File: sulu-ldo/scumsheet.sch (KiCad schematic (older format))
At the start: 19 parts, among them J10 through_hole, J11 through_hole, J12 through_hole, J13 through_hole, J14 through_hole, J15 through_hole, J16 through_hole, J17 through_hole, J18 through_hole, J19 through_hole, J20 through_hole, J21 through_hole, J5 through_hole, J6 through_hole, J7 through_hole, J8 through_hole, J9 through_hole, U1 scum3

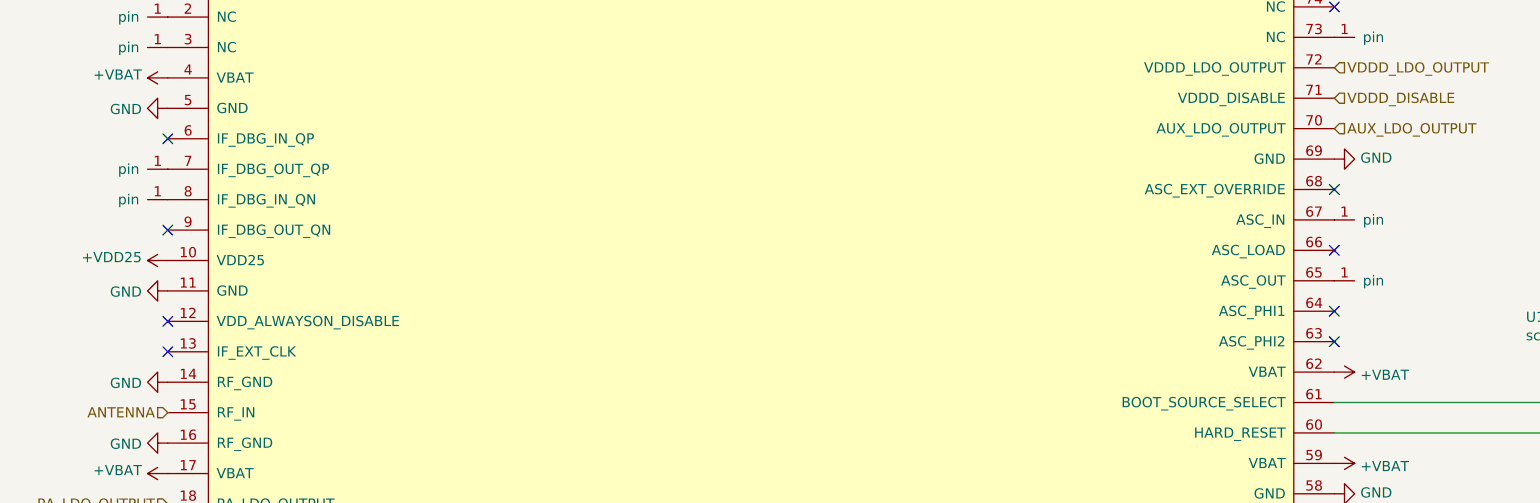
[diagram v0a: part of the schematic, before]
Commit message: added ldos
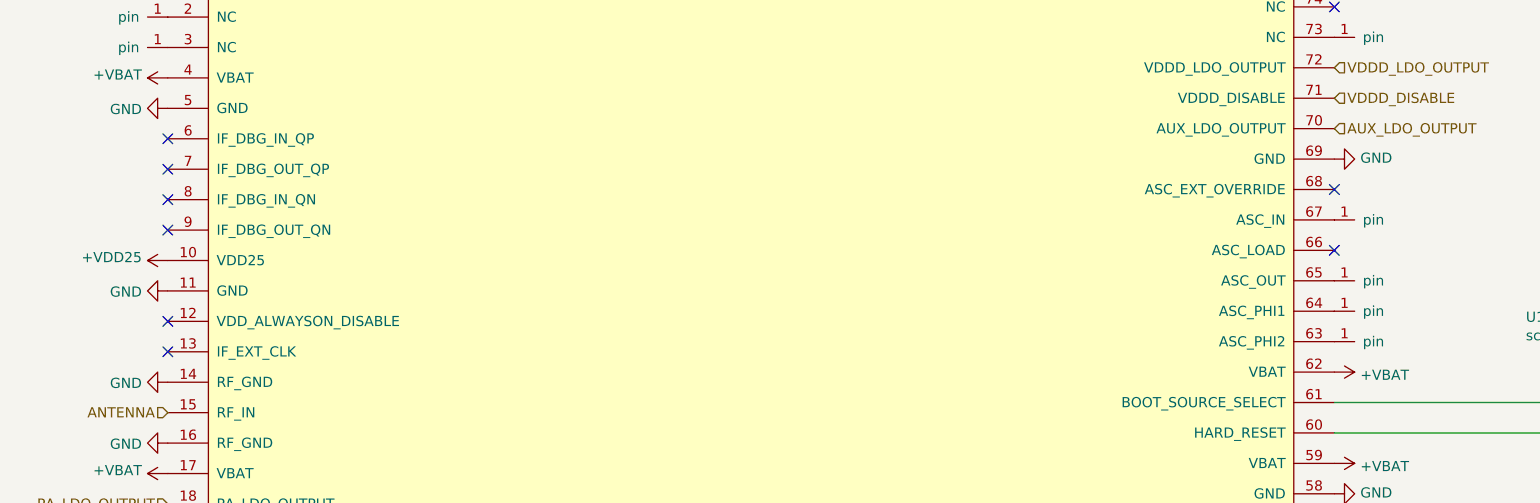
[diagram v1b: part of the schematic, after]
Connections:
- net at U1.63 (ASC_PHI2): now also J9.1 (pin)
- net at U1.64 (ASC_PHI1): now also J10.1 (pin)
- net at U1.7 (IF_DBG_OUT_QP): no longer J9.1 (pin)
- net at U1.8 (IF_DBG_IN_QN): no longer J10.1 (pin)
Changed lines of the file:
@@
 NoConn ~ 8000 3000
 NoConn ~ 8000 3300
-NoConn ~ 8000 3600
-NoConn ~ 8000 3750
 Text HLabel 6750 6050 3    50   BiDi ~ 0
 3WB_CLK
@@
 L draft1library:through_hole J9
 U 1 1 60914928
-P 2250 2900
-F 0 "J9" H 2250 3100 50  0001 C CNN
-F 1 "through_hole" H 2250 3000 50  0001 C CNN
-F 2 "SCUM:through_hole" H 2250 2900 50  0001 C CNN
-F 3 "" H 2250 2900 50  0001 C CNN
-	1    2250 2900
-	-1   0    0    1
+P 8000 3750
+F 0 "J9" H 8000 3950 50  0001 C CNN
+F 1 "through_hole" H 8000 3850 50  0001 C CNN
+F 2 "SCUM:through_hole" H 8000 3750 50  0001 C CNN
+F 3 "" H 8000 3750 50  0001 C CNN
+	1    8000 3750
+	1    0    0    -1
 $EndComp
 $Comp
 L draft1library:through_hole J10
 U 1 1 60914AFA
-P 2250 3050
-F 0 "J10" H 2250 3250 50  0001 C CNN
-F 1 "through_hole" H 2250 3150 50  0001 C CNN
-F 2 "SCUM:through_hole" H 2250 3050 50  0001 C CNN
-F 3 "" H 2250 3050 50  0001 C CNN
-	1    2250 3050
-	-1   0    0    1
+P 8000 3600
+F 0 "J10" H 8000 3800 50  0001 C CNN
+F 1 "through_hole" H 8000 3700 50  0001 C CNN
+F 2 "SCUM:through_hole" H 8000 3600 50  0001 C CNN
+F 3 "" H 8000 3600 50  0001 C CNN
+	1    8000 3600
+	1    0    0    -1
 $EndComp
 $Comp
@@
 Wire Wire Line
 	5000 1000 5000 1150
+NoConn ~ 2250 2900
+NoConn ~ 2250 3050
 $EndSCHEMATC
